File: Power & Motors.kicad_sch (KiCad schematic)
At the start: 43 parts, among them J4 Conn_01x03_Pin, J5 Conn_01x03_Pin, J6 Conn_01x03_Pin, U2 MIC5504-3.3YM5, U3 AP62300TWU

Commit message: Ready to finalize Rev3
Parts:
- added D10, D9: D_Zener3.3V, Diode_SMD:D_SOD-123, symbol Device:D_Zener
- added D11, D12: D_Zener5V, Diode_SMD:D_SOD-123, symbol Device:D_Zener
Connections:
- net +3V3: now also D10.1 (K), D9.1 (K)
- net +5V: now also D11.1 (K), D12.1 (K)
- net GND: now also D10.2 (A), D11.2 (A), D12.2 (A), D9.2 (A)
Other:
- note added: "Overvoltage Protection"
- moved on the sheet: Battery1, C10, C5, C6, C7, C8, C9, D2, D3, D4, D5, D6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

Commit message: Rev3 ready to order
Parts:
- C7: value C0.1uF -> C1uF; DigiKey C1206C104K5RAC7800 -> CL31B105KBHNNNE
- C8: value C10uF -> C22uF; DigiKey CL31B106KOHNNWE -> CL31A226MOCLNNC
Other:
- note added: ""Bypass VIN to GND with a suitably large capacitor""
- note added: "SW to BST capacitor: "100nF or higher""
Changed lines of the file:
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@@
 		)
 	)
+	(text "\"Bypass VIN to GND with\na suitably large capacitor\""
+		(exclude_from_sim no)
+		(at 35.306 25.4 0)
+		(effects
+			(font
+				(size 1.27 1.27)
+			)
+			(justify left bottom)
+		)
+	)
 	(text "Overvoltage Protection"
 		(exclude_from_sim no)
@@
 		)
 	)
+	(text "SW to BST capacitor:\n\"100nF or higher\""
+		(exclude_from_sim no)
+		(at 64.77 48.514 0)
+		(effects
+			(font
+				(size 1.27 1.27)
+			)
+			(justify left bottom)
+		)
+	)
 	(text "VIN: 4.2 to 18V"
 		(exclude_from_sim no)
-		(at 41.91 22.86 0)
+		(at 34.29 19.304 0)
 		(effects
 			(font
@@
 			)
 		)
-		(property "Value" "C0.1uF"
+		(property "Value" "C1uF"
 			(at 78.74 38.1062 0)
 			(effects
@@
 			)
 		)
-		(property "DigiKey" "C1206C104K5RAC7800"
+		(property "DigiKey" "CL31B105KBHNNNE"
 			(at 76.2 36.83 0)
 			(effects
@@
 			)
 		)
-		(property "Value" "C10uF"
+		(property "Value" "C22uF"
 			(at 39.37 46.9963 0)
 			(effects
@@
 			)
 		)
-		(property "DigiKey" "CL31B106KOHNNWE"
+		(property "DigiKey" "CL31A226MOCLNNC"
 			(at 41.91 45.72 0)
 			(effects

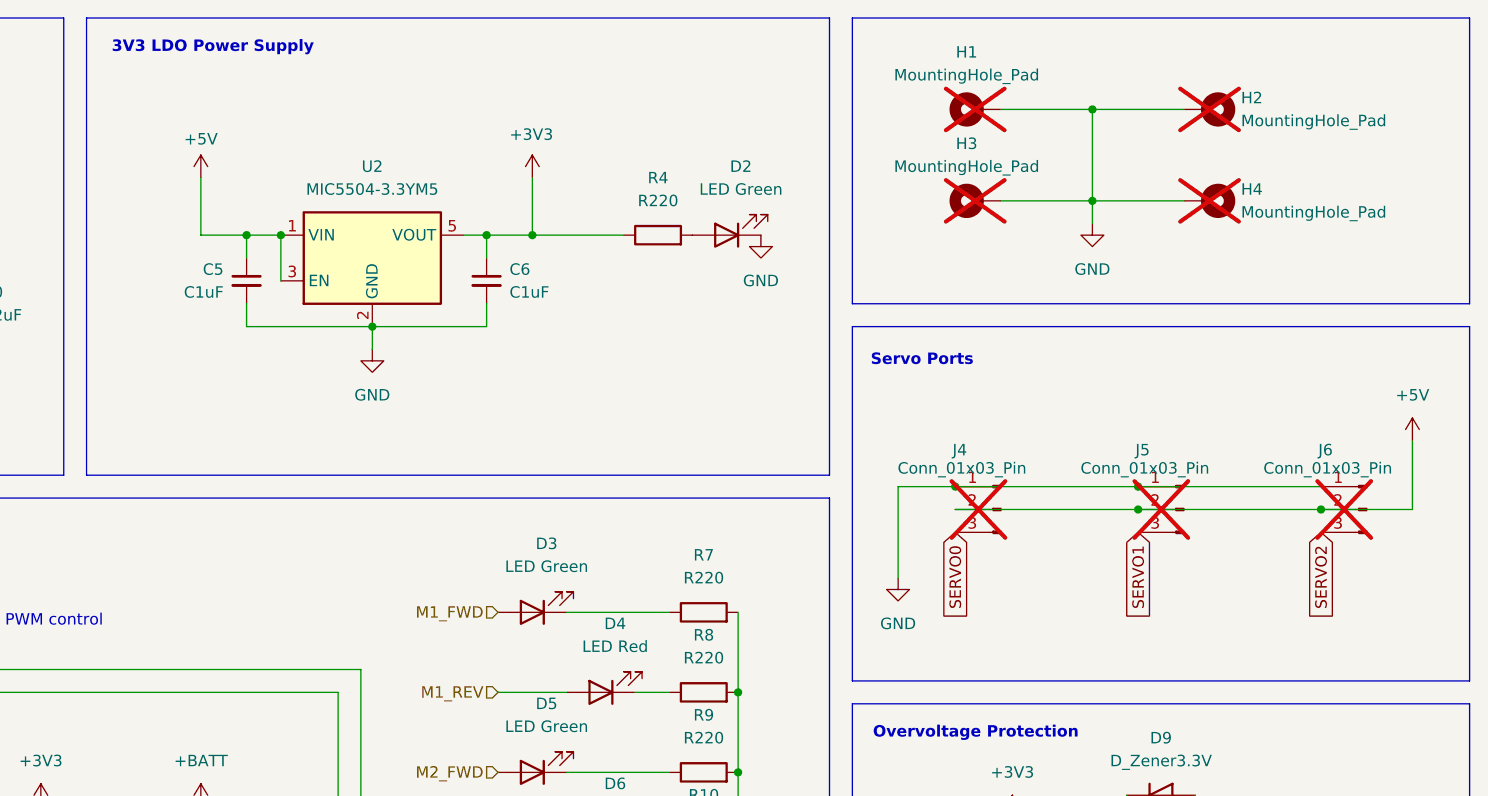
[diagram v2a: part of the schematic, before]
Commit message: Rewire the entire thing to use hardware PWM and software quadrature decoding
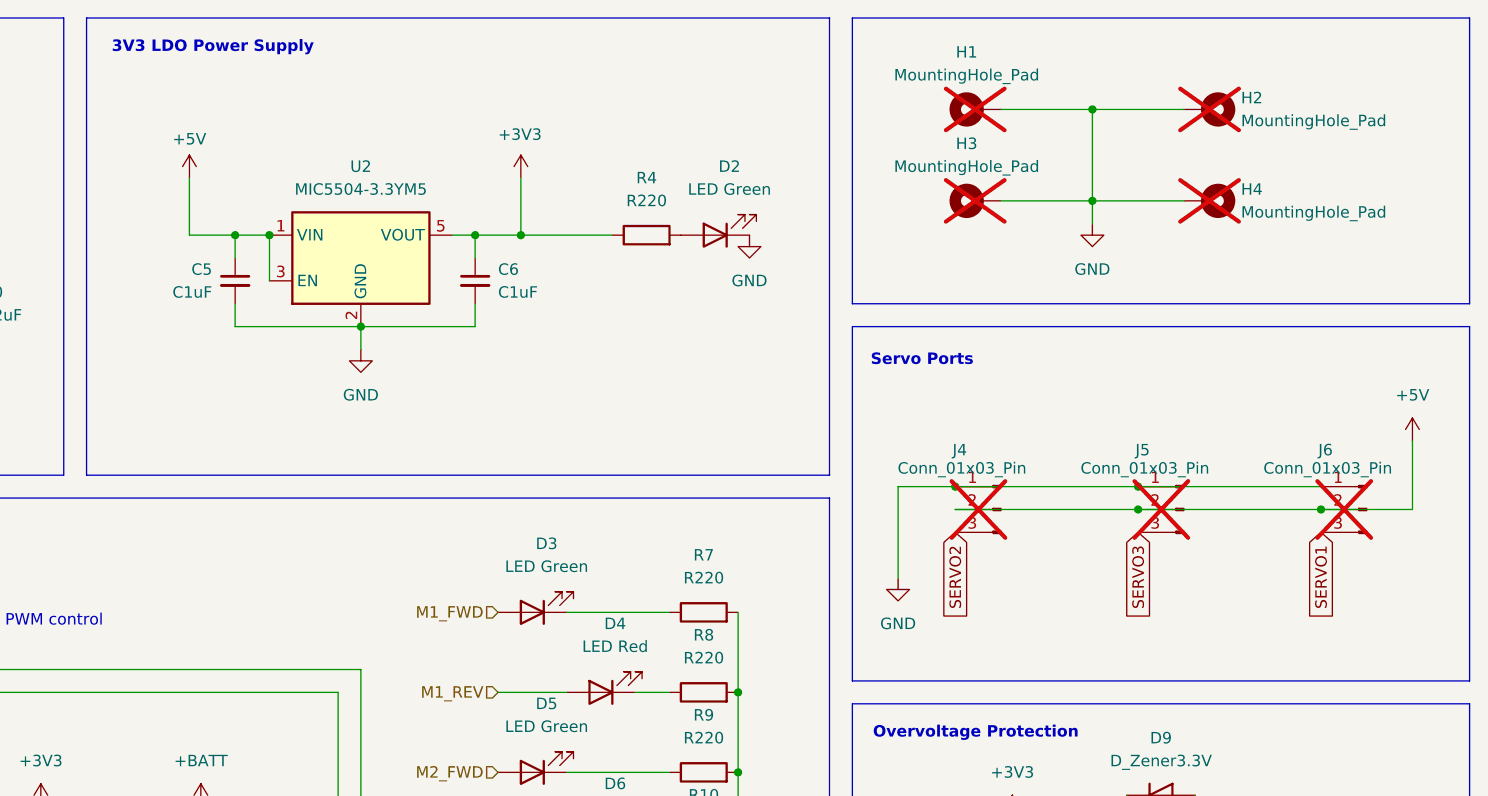
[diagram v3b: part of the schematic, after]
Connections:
- net SERVO0 is gone; now on net SERVO2: J4.3 (Pin_3)
- net SERVO1: now also J6.3 (Pin_3); no longer J5.3 (Pin_3)
- net SERVO2: no longer J6.3 (Pin_3)
- new net SERVO3: J5.3 (Pin_3)
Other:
- moved on the sheet: C5, C6, D2, R4, U2

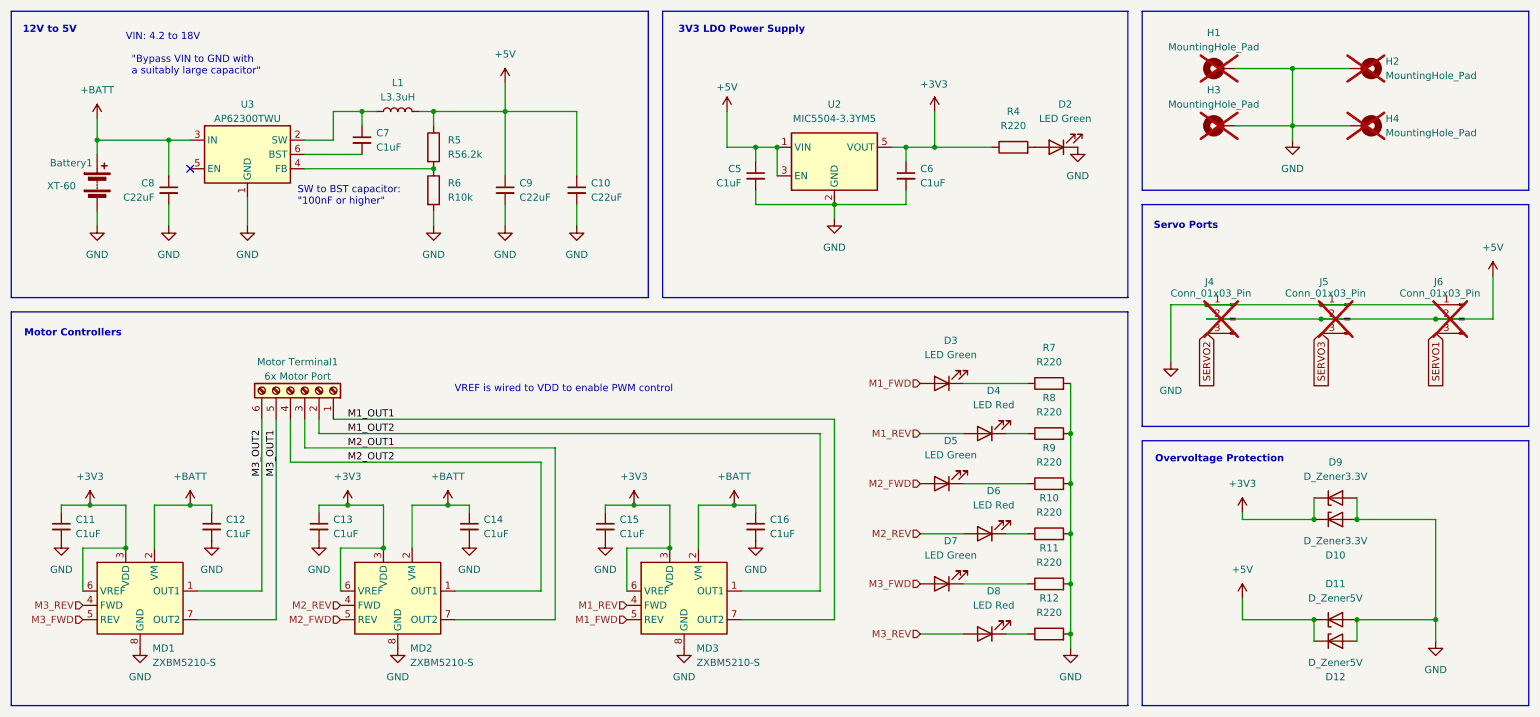
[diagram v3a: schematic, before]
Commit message: change to ESP32-C6-WROOM
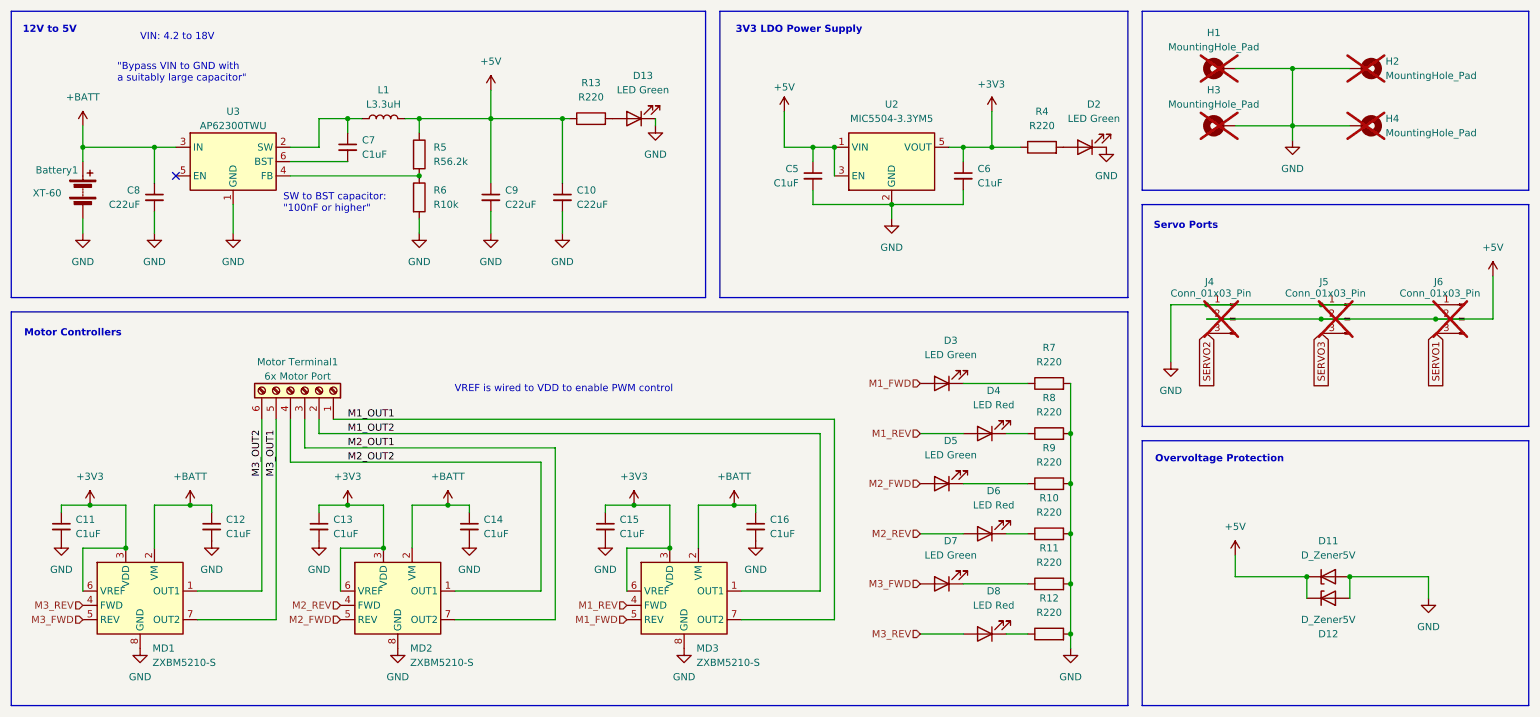
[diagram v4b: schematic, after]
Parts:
- removed D10, D9: D_Zener3.3V, Diode_SMD:D_SOD-123, symbol Device:D_Zener
- added D13: LED Green, LED_SMD:LED_1206_3216Metric_Pad1.42x1.75mm_HandSolder, symbol Device:LED
- added R13: R220, Resistor_SMD:R_1206_3216Metric_Pad1.30x1.75mm_HandSolder, symbol Device:R
- R6: DigiKey RC1206FR-0710KL -> RMCF1206FT10K0
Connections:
- net +5V: now also R13.1
- net GND: now also D13.1 (K)
- new net: D13.2 (A), R13.2
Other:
- moved on the sheet: Battery1, C10, C5, C6, C7, C8, C9, D11, D12, D2, L1, R4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

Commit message: i forgor
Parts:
- Battery1, D11, D12: now not fitted
- C10, C8, C9: value C22uF -> 22uF
- C11, C12, C13, C14, C15, C16, C5, C6, C7: value C1uF -> 1uF
- L1: value L3.3uH -> 3.3uH
- Motor Terminal1: now not fitted
- R10, R11, R12, R13, R4, R7, R8, R9: value R220 -> 220
- R5: value R56.2k -> 56.2k
- R6: value R10k -> 10k
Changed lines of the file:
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@@
 			)
 		)
-		(property "Value" "C1uF"
+		(property "Value" "1uF"
 			(at 76.2 39.3762 0)
 			(effects
@@
 			)
 		)
-		(property "Value" "R220"
+		(property "Value" "220"
 			(at 116.84 29.21 90)
 			(effects
@@
 			)
 		)
-		(property "Value" "R220"
+		(property "Value" "220"
 			(at 198.12 120.65 90)
 			(effects
@@
 			)
 		)
-		(property "Value" "R10k"
+		(property "Value" "10k"
 			(at 88.9 48.26 0)
 			(effects
@@
 			)
 		)
-		(property "Value" "R220"
+		(property "Value" "220"
 			(at 198.12 85.09 90)
 			(effects
@@
 		(in_bom yes)
 		(on_board yes)
-		(dnp no)
+		(dnp yes)
 		(property "Reference" "D11"
 			(at 247.65 107.95 0)
@@
 			)
 		)
-		(property "Value" "C1uF"
+		(property "Value" "1uF"
 			(at 121.92 106.6863 0)
 			(effects
@@
 			)
 		)
-		(property "Value" "C1uF"
+		(property "Value" "1uF"
 			(at 71.12 106.6863 0)
 			(effects
@@
 			)
 		)
-		(property "Value" "R220"
+		(property "Value" "220"
 			(at 198.12 111.76 90)
 			(effects
@@
 		(in_bom yes)
 		(on_board yes)
-		(dnp no)
+		(dnp yes)
 		(fields_autoplaced yes)
 		(property "Reference" "Motor Terminal1"
@@
 			)
 		)
-		(property "Value" "C22uF"
+		(property "Value" "22uF"
 			(at 36.83 48.2663 0)
 			(effects
@@
 		(in_bom yes)
 		(on_board yes)
-		(dnp no)
+		(dnp yes)
 		(property "Reference" "D12"
 			(at 247.65 124.46 0)
@@
 		(in_bom yes)
 		(on_board yes)
-		(dnp no)
+		(dnp yes)
 		(property "Reference" "Battery1"
 			(at 18.288 42.164 0)
@@
 			)
 		)
-		(property "Value" "L3.3uH"
+		(property "Value" "3.3uH"
 			(at 80.01 30.48 90)
 			(effects
@@
 			)
 		)
-		(property "Value" "R220"
+		(property "Value" "220"
 			(at 196.85 34.29 90)
 			(effects
@@
 			)
 		)
-		(property "Value" "R220"
+		(property "Value" "220"
 			(at 198.12 76.2 90)
 			(effects
@@
 			)
 		)
-		(property "Value" "C1uF"
+		(property "Value" "1uF"
 			(at 25.4 106.6863 0)
 			(effects
@@
 			)
 		)
-		(property "Value" "R56.2k"
+		(property "Value" "56.2k"
 			(at 88.9 40.6399 0)
 			(effects
@@
 			)
 		)
-		(property "Value" "C1uF"
+		(property "Value" "1uF"
 			(at 97.79 106.6863 0)
 			(effects
@@
 			)
 		)
-		(property "Value" "C1uF"
+		(property "Value" "1uF"
 			(at 148.59 106.6863 0)
 			(effects
@@
 			)
 		)
-		(property "Value" "R220"
+		(property "Value" "220"
 			(at 198.12 93.98 90)
 			(effects
@@
 			)
 		)
-		(property "Value" "C22uF"
+		(property "Value" "22uF"
 			(at 101.6 48.2662 0)
 			(effects
@@
 			)
 		)
-		(property "Value" "C1uF"
+		(property "Value" "1uF"
 			(at 52.07 106.6863 0)
 			(effects
@@
 			)
 		)
-		(property "Value" "R220"
+		(property "Value" "220"
 			(at 198.12 102.87 90)
 			(effects
@@
 			)
 		)
-		(property "Value" "C1uF"
+		(property "Value" "1uF"
 			(at 185.42 44.4563 0)
 			(effects
@@
 			)
 		)
-		(property "Value" "C1uF"
+		(property "Value" "1uF"
 			(at 153.67 44.4563 0)
 			(effects
@@
 			)
 		)
-		(property "Value" "C22uF"
+		(property "Value" "22uF"
 			(at 114.3 48.2662 0)
 			(effects
